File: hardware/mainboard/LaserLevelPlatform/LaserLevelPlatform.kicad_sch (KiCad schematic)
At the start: 45 parts, among them J1 Conn_01x04_Male, J2 Conn_01x04_Male, J3 Conn_02x04_Odd_Even, J4 Conn_01x02_Male, J5 Conn_01x02_Female, J6 Conn_01x02_Male, J7 Conn_01x02_Male, U1 Lolin32, U2 DCDC

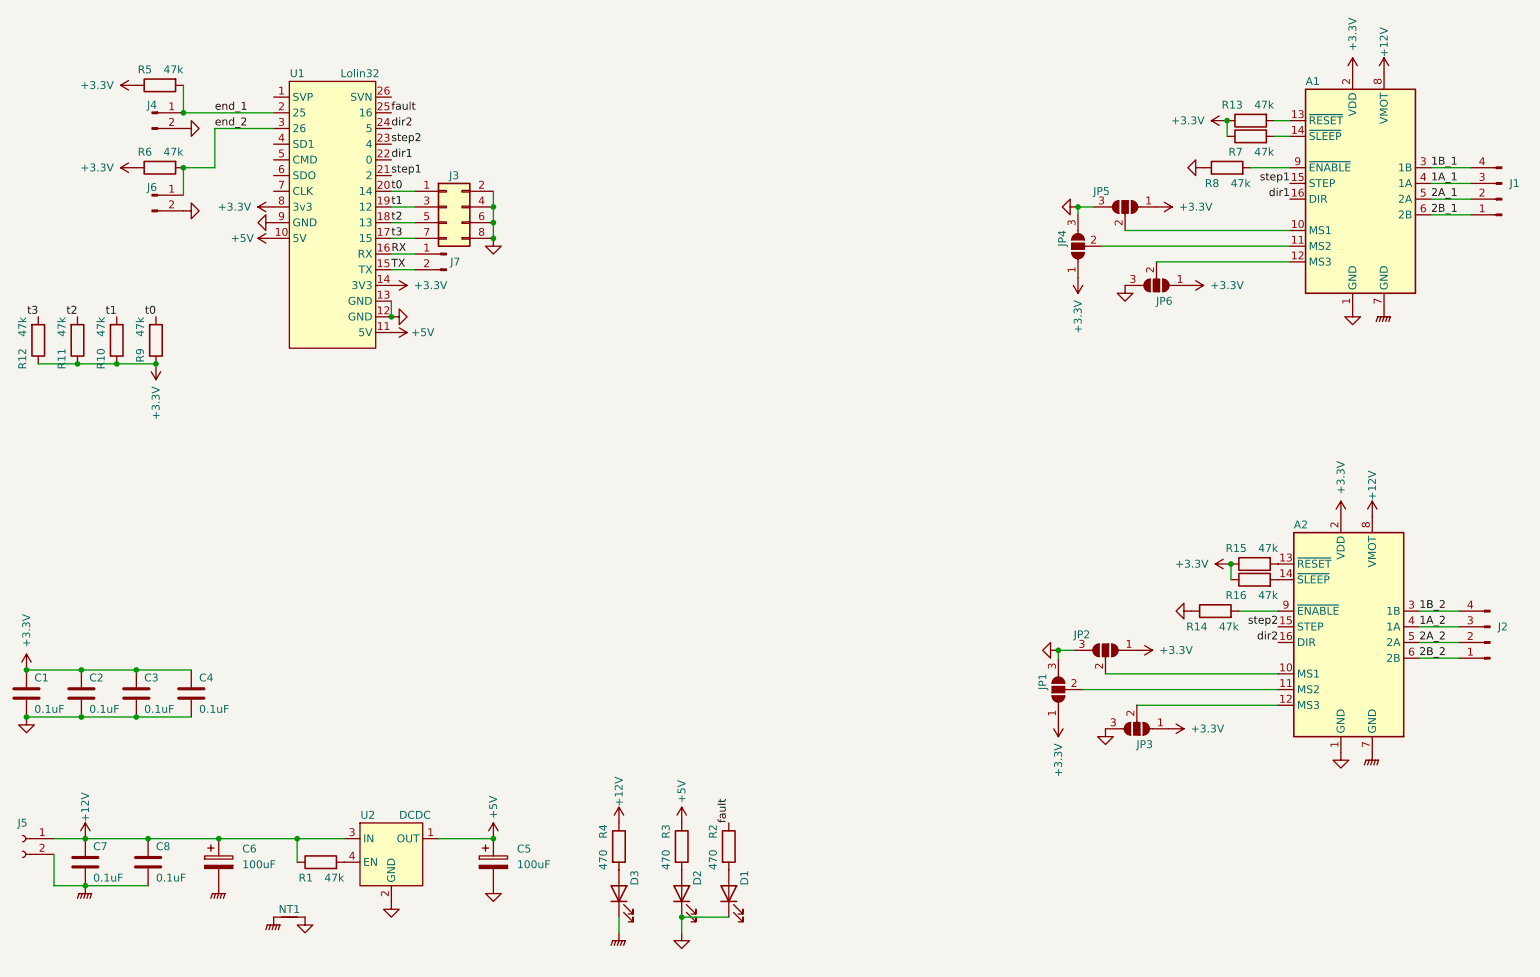
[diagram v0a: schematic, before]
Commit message: Add jumper on +5V line
Add a jumper to disconnect +5V power line from DC-DC converter from the
main CPU board. This is needed for safe connection of a USB power
together with a +12V input. Also added a bridge in parallel to it for
the permanent connection.
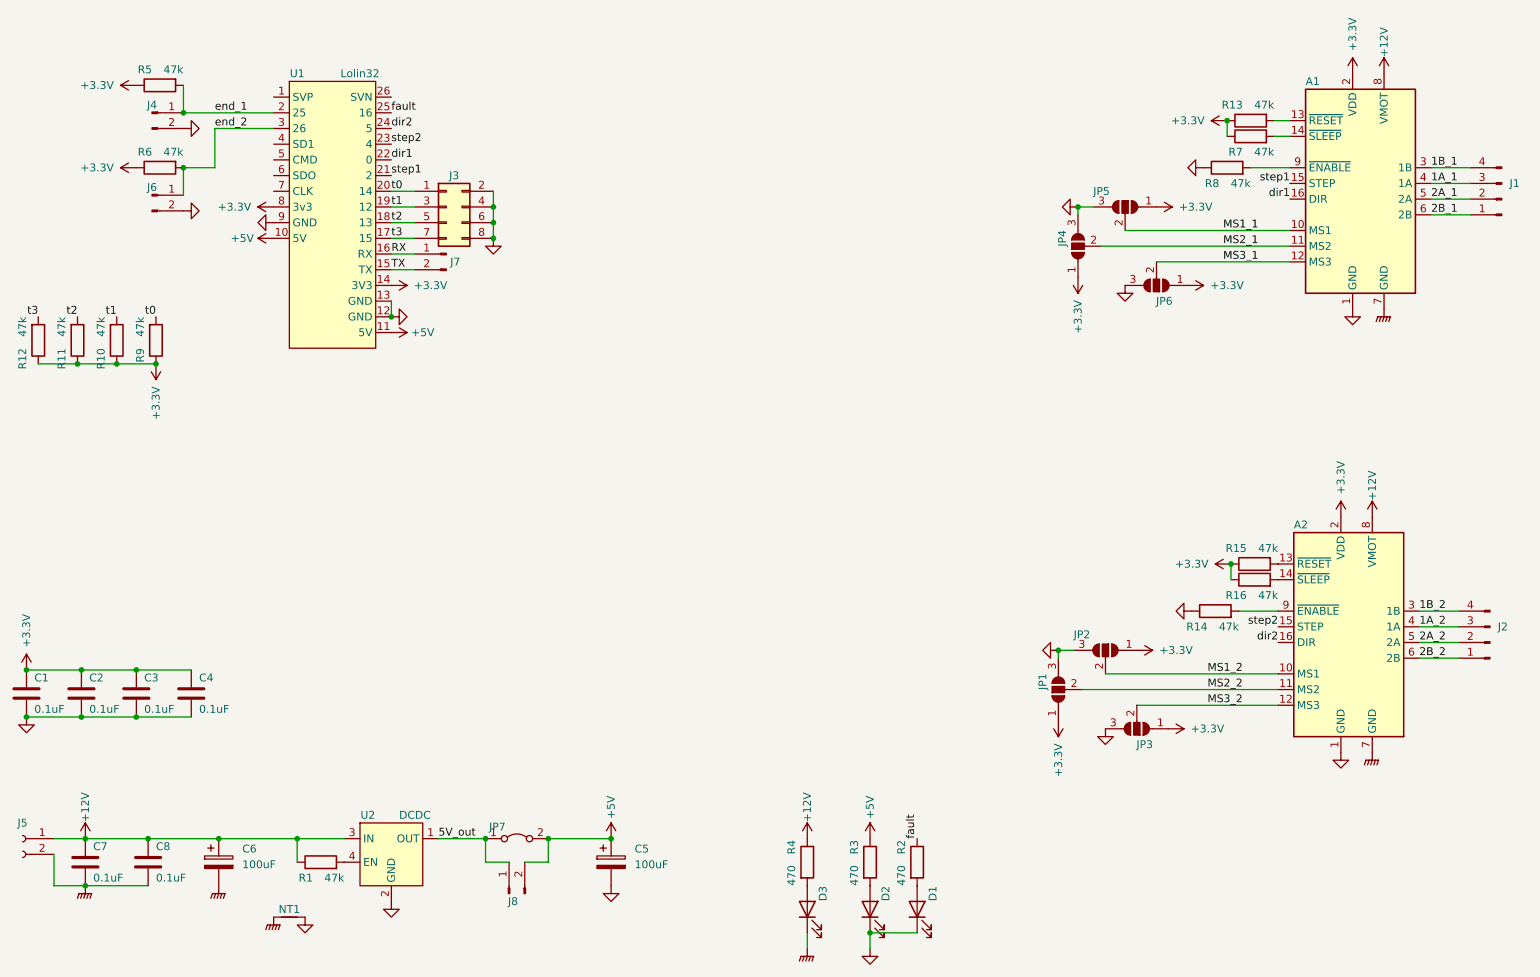
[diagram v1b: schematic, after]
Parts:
- added J8: Conn_01x02_Male, Connector_PinHeader_2.54mm:PinHeader_1x02_P2.54mm_Vertical, symbol Connector:Conn_01x02_Male
- added JP7: Jumper_2_Bridged, Jumper:SolderJumper-2_P1.3mm_Open_TrianglePad1.0x1.5mm, symbol Jumper:Jumper_2_Bridged
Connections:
- net +5V: now also J8.2 (Pin_2), JP7.2 (B); no longer U2.1 (OUT)
- net MS1_1: now reaches A1.10 (MS1), JP5.2 (C)
- net MS2_2: now reaches A2.11 (MS2), JP1.2 (C)
- net MS2_1: now reaches A1.11 (MS2), JP4.2 (C)
- net MS3_1: now reaches A1.12 (MS3), JP6.2 (C)
- net MS3_2: now reaches A2.12 (MS3), JP3.2 (C)
- net MS1_2: now reaches A2.10 (MS1), JP2.2 (C)
- new net 5V_out: J8.1 (Pin_1), JP7.1 (A), U2.1 (OUT)
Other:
- moved on the sheet: C5, D1, D2, D3, R2, R3, R4
